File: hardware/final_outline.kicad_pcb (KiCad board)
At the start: 2 copper layers, 99.5 x 75 mm, 31 parts, among them P001 CANCONNECTOR, P002 CONN_01X14, P100 ISP, P101 DEBUG_LED, U401 MCP2551-I/SN, U403 LPC11C14, U501 MCP1755-33, U502 MCP1755-5, U503 Zsr1000gta

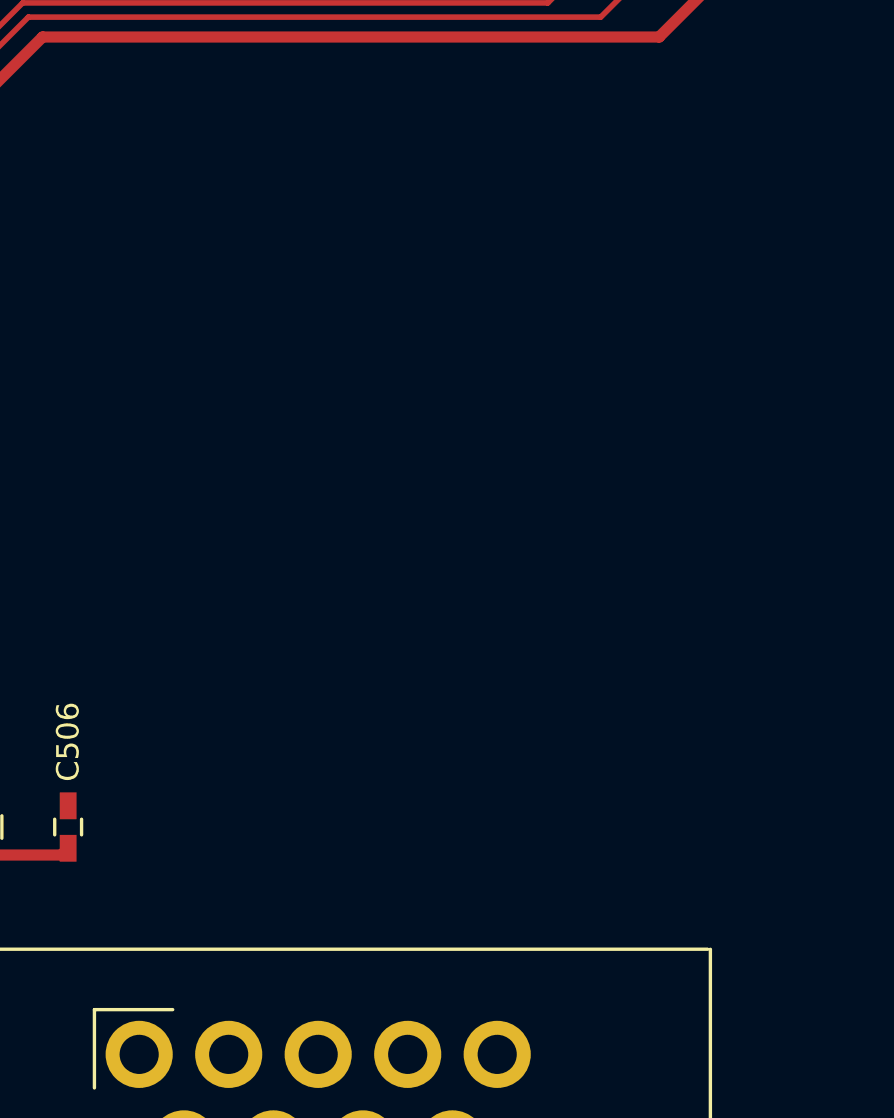
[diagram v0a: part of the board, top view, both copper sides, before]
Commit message: Fixed renaming issue in schematic, laid out components in pcb.
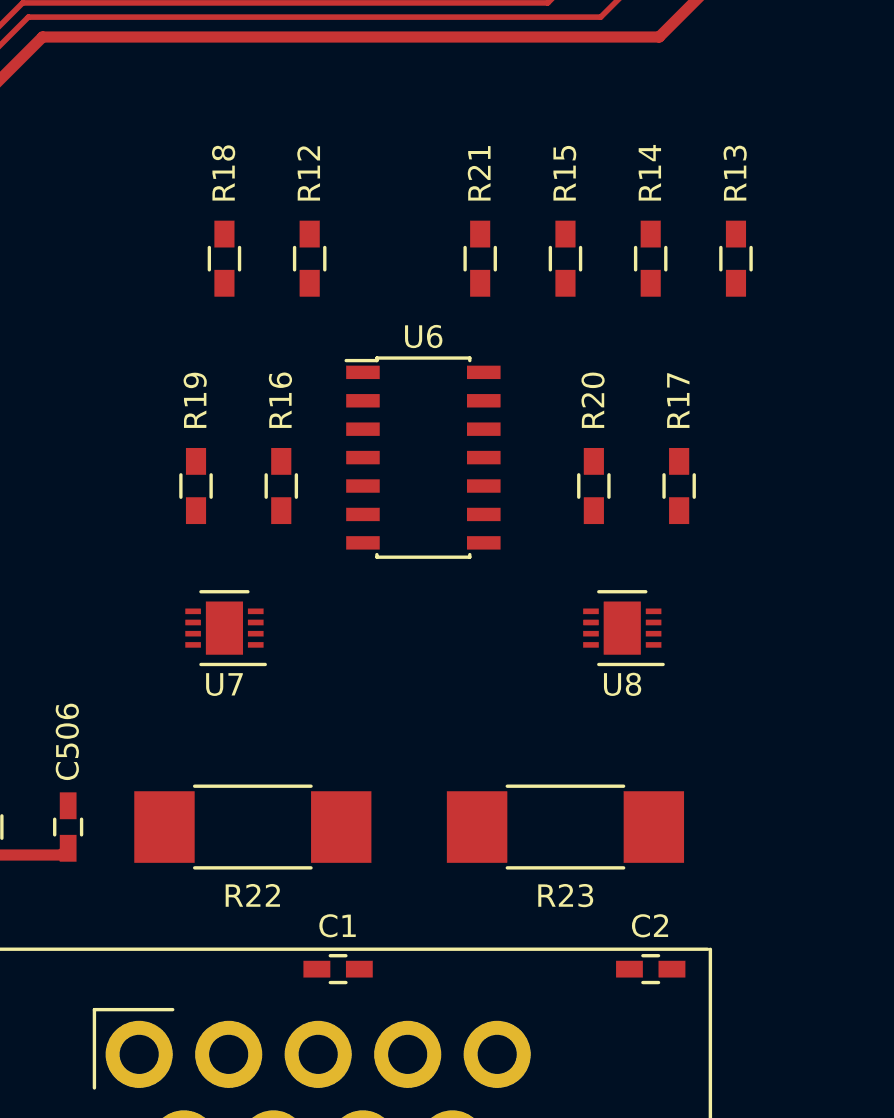
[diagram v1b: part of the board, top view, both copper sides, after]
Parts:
- added C1: 1uF, Capacitors_SMD:C_0603_HandSoldering, F.Cu at (171.4, 110.5)
- added C2: 1uF, Capacitors_SMD:C_0603_HandSoldering, F.Cu at (185.4, 110.5)
- added R12: 10k, Resistors_SMD:R_0603_HandSoldering, F.Cu at (170.2, 78.7)
- added R13: 10k, Resistors_SMD:R_0603_HandSoldering, F.Cu at (189.2, 78.7)
- added R14: 10k, Resistors_SMD:R_0603_HandSoldering, F.Cu at (185.4, 78.7)
- added R15: 10k, Resistors_SMD:R_0603_HandSoldering, F.Cu at (181.6, 78.7)
- added R16: 10k, Resistors_SMD:R_0603_HandSoldering, F.Cu at (168.9, 88.9)
- added R17: 10k, Resistors_SMD:R_0603_HandSoldering, F.Cu at (186.7, 88.9)
- added R18: 10k, Resistors_SMD:R_0603_HandSoldering, F.Cu at (166.4, 78.7)
- added R19: 10k, Resistors_SMD:R_0603_HandSoldering, F.Cu at (165.1, 88.9)
- added R20: 10k, Resistors_SMD:R_0603_HandSoldering, F.Cu at (182.9, 88.9)
- added R21: 10k, Resistors_SMD:R_0603_HandSoldering, F.Cu at (177.8, 78.7)
- added R22: 0.002, Resistors_SMD:R_2512_HandSoldering, F.Cu at (167.6, 104.1)
- added R23: 0.002, Resistors_SMD:R_2512_HandSoldering, F.Cu at (181.6, 104.1)
- added U6: TCA9543A, Housings_SOIC:SOIC-14_3.9x8.7mm_Pitch1.27mm, F.Cu at (175.3, 87.6)
- added U7: LTC2943, Housings_DFN_QFN:DFN-8-1EP_3x3mm_Pitch0.5mm, F.Cu at (166.4, 95.2)
- added U8: LTC2943, Housings_DFN_QFN:DFN-8-1EP_3x3mm_Pitch0.5mm, F.Cu at (184.2, 95.2)
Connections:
- P002 pad 1: Net-(P002-Pad1) -> /BACK_PANEL/CS_SENSE-
- P002 pad 2: Net-(P002-Pad2) -> /BACK_PANEL/CS_SENSE+
- P002 pad 4: Net-(P002-Pad4) -> /BACK_PANEL/LV_SENSE-
- P002 pad 5: Net-(P002-Pad5) -> /BACK_PANEL/LV_SENSE+
- P002 pad 6: Net-(P002-Pad6) -> /BACK_PANEL/CS_SENSE-
- P002 pad 7: Net-(P002-Pad7) -> /BACK_PANEL/CS_SENSE+
- P002 pad 8: Net-(P002-Pad8) -> /BACK_PANEL/LV_SENSE-
- P002 pad 9: Net-(P002-Pad9) -> /BACK_PANEL/LV_SENSE+
- U403 pad 15: /Micro_Controller/PIO0_4 -> /I2C Multiplexer and Gas Gauges/SCL
- U403 pad 16: /Micro_Controller/PIO0_5 -> /I2C Multiplexer and Gas Gauges/SDA

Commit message: Finished laying out PCB and completed traces.
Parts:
- moved C1 2.84 mm to (172.7, 108.0)
- moved C2 2.84 mm to (186.7, 108.0)
- moved R21 2.54 mm to (175.3, 78.7)
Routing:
- net /I2C Multiplexer and Gas Gauges/SCL: track 0.00 -> 115.0 mm, vias 0 -> 2
- net /I2C Multiplexer and Gas Gauges/SDA: track 0.00 -> 108.1 mm, vias 0 -> 2
- net +5V: track 113.2 -> 197.7 mm
- net /BACK_PANEL/CS_SENSE+: track 0.00 -> 26.9 mm
- net /BACK_PANEL/LV_SENSE+: track 0.00 -> 26.7 mm
- net /BACK_PANEL/LV_SENSE-: track 0.00 -> 26.5 mm
- net /BACK_PANEL/CS_SENSE-: track 0.00 -> 25.7 mm
- net Net-(R13-Pad2): track 0.00 -> 17.0 mm
- net Net-(R17-Pad2): track 0.00 -> 14.2 mm
- net Net-(R21-Pad2): track 0.00 -> 13.6 mm
- net Net-(R19-Pad2): track 0.00 -> 12.5 mm
- net Net-(R18-Pad2): track 0.00 -> 11.4 mm
- net GND: track 29.1 -> 39.3 mm, vias 6 -> 8
- net Net-(R20-Pad2): track 0.00 -> 9.54 mm
- net Net-(R16-Pad2): track 0.00 -> 8.69 mm
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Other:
- rule pad_to_mask_clearance: 0.2 -> 0.02

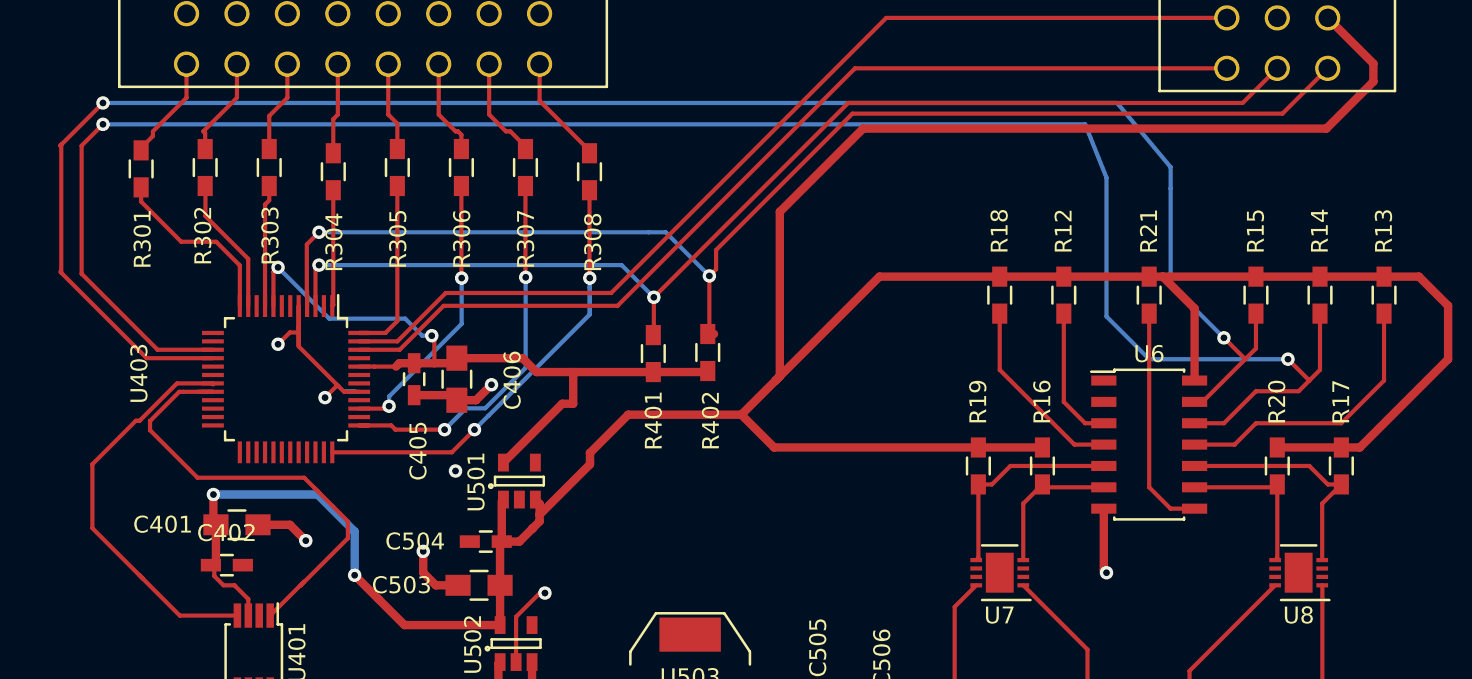
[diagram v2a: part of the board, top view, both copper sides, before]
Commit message: Finished PCB layout for real this time.
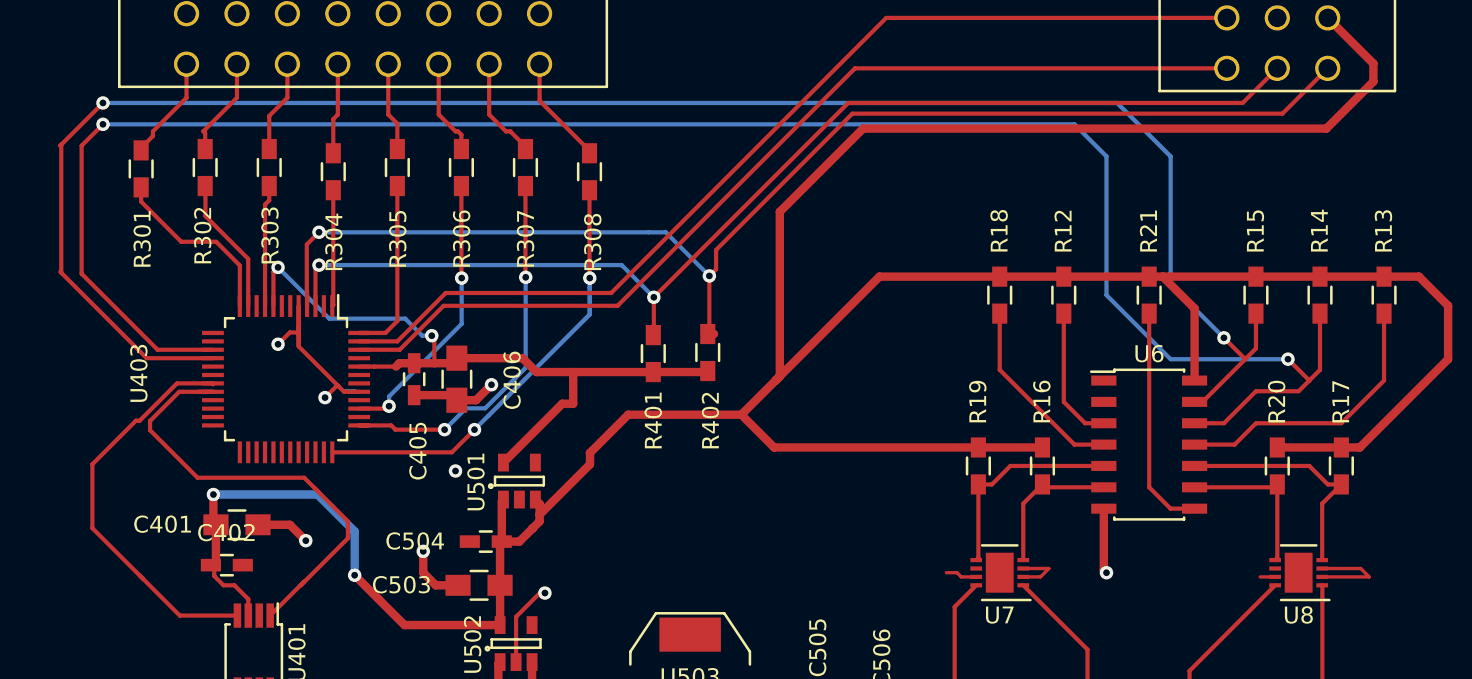
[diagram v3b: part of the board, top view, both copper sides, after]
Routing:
- net GND: track 39.3 -> 51.1 mm
- net /I2C Multiplexer and Gas Gauges/SCL: track 115.0 -> 114.1 mm
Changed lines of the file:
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@@
   (general
     (links 133)
-    (no_connects 6)
+    (no_connects 0)
     (area 102.424999 49.875 215 136.899792)
     (thickness 1.6)
     (drawings 6)
-    (tracks 432)
+    (tracks 441)
     (zones 0)
     (modules 48)
@@
   (segment (start 141.97 70.15) (end 141.97 70.3) (width 0.25) (layer F.Cu) (net 5))
   (segment (start 139 67.18) (end 141.97 70.15) (width 0.25) (layer F.Cu) (net 5))
+  (segment (start 182.75 95.5) (end 181.86 95.5) (width 0.2) (layer F.Cu) (net 6))
+  (segment (start 188.345 95.5) (end 187.845 95) (width 0.2) (layer F.Cu) (net 6))
+  (segment (start 187.845 95) (end 185.55 95) (width 0.2) (layer F.Cu) (net 6))
+  (segment (start 185.55 95.5) (end 188.345 95.5) (width 0.2) (layer F.Cu) (net 6))
+  (segment (start 163.83 95.25) (end 163.195 95.25) (width 0.2) (layer F.Cu) (net 6))
+  (segment (start 164.08 95.5) (end 163.83 95.25) (width 0.2) (layer F.Cu) (net 6))
+  (segment (start 164.97 95.5) (end 164.08 95.5) (width 0.2) (layer F.Cu) (net 6))
+  (segment (start 169.295 95) (end 168.795 95.5) (width 0.2) (layer F.Cu) (net 6))
+  (segment (start 168.795 95.5) (end 167.77 95.5) (width 0.2) (layer F.Cu) (net 6))
+  (segment (start 167.77 95) (end 169.295 95) (width 0.2) (layer F.Cu) (net 6))
   (segment (start 187.64 107.95) (end 188.595 107.95) (width 0.5) (layer F.Cu) (net 6))
   (via (at 192.405 104.14) (size 0.8) (drill 0.4) (layers F.Cu B.Cu) (net 6))
@@
   (segment (start 189.23 83.82) (end 186.69 86.36) (width 0.25) (layer F.Cu) (net 72))
   (segment (start 189.23 79.84) (end 189.23 80.01) (width 0.25) (layer F.Cu) (net 72))
-  (segment (start 113.03 68.58) (end 111.76 69.85) (width 0.25) (layer F.Cu) (net 73))
-  (segment (start 183.515 82.55) (end 175.26 82.55) (width 0.25) (layer B.Cu) (net 73))
-  (via (at 183.515 82.55) (size 0.8) (drill 0.4) (layers F.Cu B.Cu) (net 73))
-  (segment (start 184.785 83.82) (end 183.515 82.55) (width 0.25) (layer F.Cu) (net 73))
-  (segment (start 113.03 68.58) (end 171.45 68.58) (width 0.25) (layer B.Cu) (net 73))
-  (segment (start 172.72 71.755) (end 171.45 68.58) (width 0.25) (layer B.Cu) (net 73))
-  (segment (start 172.72 80.01) (end 172.72 71.755) (width 0.25) (layer B.Cu) (net 73))
-  (segment (start 175.26 82.55) (end 172.72 80.01) (width 0.25) (layer B.Cu) (net 73))
+  (segment (start 183.515 82.55) (end 176.53 82.55) (width 0.25) (layer B.Cu) (net 73))
   (via (at 113.03 68.58) (size 0.8) (drill 0.4) (layers F.Cu B.Cu) (net 73))
-  (segment (start 116.28 81.99) (end 119.57 81.99) (width 0.25) (layer F.Cu) (net 73))
+  (segment (start 119.57 81.99) (end 116.28 81.99) (width 0.25) (layer F.Cu) (net 73))
   (segment (start 111.76 77.47) (end 116.28 81.99) (width 0.25) (layer F.Cu) (net 73))
   (segment (start 111.76 69.85) (end 111.76 77.47) (width 0.25) (layer F.Cu) (net 73))
+  (segment (start 113.03 68.58) (end 111.76 69.85) (width 0.25) (layer F.Cu) (net 73))
+  (segment (start 172.72 70.485) (end 170.815 68.58) (width 0.25) (layer B.Cu) (net 73))
+  (segment (start 113.03 68.58) (end 170.815 68.58) (width 0.25) (layer B.Cu) (net 73))
+  (segment (start 183.515 82.55) (end 184.785 83.82) (width 0.25) (layer F.Cu) (net 73))
+  (via (at 183.515 82.55) (size 0.8) (drill 0.4) (layers F.Cu B.Cu) (net 73))
+  (segment (start 172.72 78.74) (end 172.72 70.485) (width 0.25) (layer B.Cu) (net 73))
+  (segment (start 176.53 82.55) (end 172.72 78.74) (width 0.25) (layer B.Cu) (net 73))
   (segment (start 185.42 79.84) (end 185.42 83.185) (width 0.25) (layer F.Cu) (net 73))
   (segment (start 179.705 86.36) (end 177.96 86.36) (width 0.25) (layer F.Cu) (net 73))
@@
   (segment (start 185.42 83.185) (end 184.785 83.82) (width 0.25) (layer F.Cu) (net 73))
   (segment (start 184.785 83.82) (end 184.15 84.455) (width 0.25) (layer F.Cu) (net 73))
+  (segment (start 176.53 78.105) (end 176.53 70.485) (width 0.25) (layer B.Cu) (net 74))
   (segment (start 110.55 77.41) (end 110.55 69.79) (width 0.25) (layer F.Cu) (net 74))
   (via (at 113.03 67.31) (size 0.8) (drill 0.4) (layers F.Cu B.Cu) (net 74))
-  (segment (start 176.53 71.12) (end 173.355 67.31) (width 0.25) (layer B.Cu) (net 74))
   (segment (start 113.03 67.31) (end 173.355 67.31) (width 0.25) (layer B.Cu) (net 74))
   (segment (start 179.705 81.28) (end 180.975 82.55) (width 0.25) (layer F.Cu) (net 74))
   (via (at 179.705 81.28) (size 0.8) (drill 0.4) (layers F.Cu B.Cu) (net 74))
   (segment (start 179.705 81.28) (end 176.53 78.105) (width 0.25) (layer B.Cu) (net 74))
-  (segment (start 176.53 78.105) (end 176.53 72.39) (width 0.25) (layer B.Cu) (net 74))
-  (segment (start 176.53 72.39) (end 176.53 71.12) (width 0.25) (layer B.Cu) (net 74))
   (segment (start 113.03 67.31) (end 110.49 69.85) (width 0.25) (layer F.Cu) (net 74))
   (segment (start 110.55 69.79) (end 110.49 69.85) (width 0.25) (layer F.Cu) (net 74))
+  (segment (start 173.355 67.31) (end 176.53 70.485) (width 0.25) (layer B.Cu) (net 74))
   (segment (start 119.57 82.49) (end 115.63 82.49) (width 0.25) (layer F.Cu) (net 74))
   (segment (start 115.63 82.49) (end 110.55 77.41) (width 0.25) (layer F.Cu) (net 74))

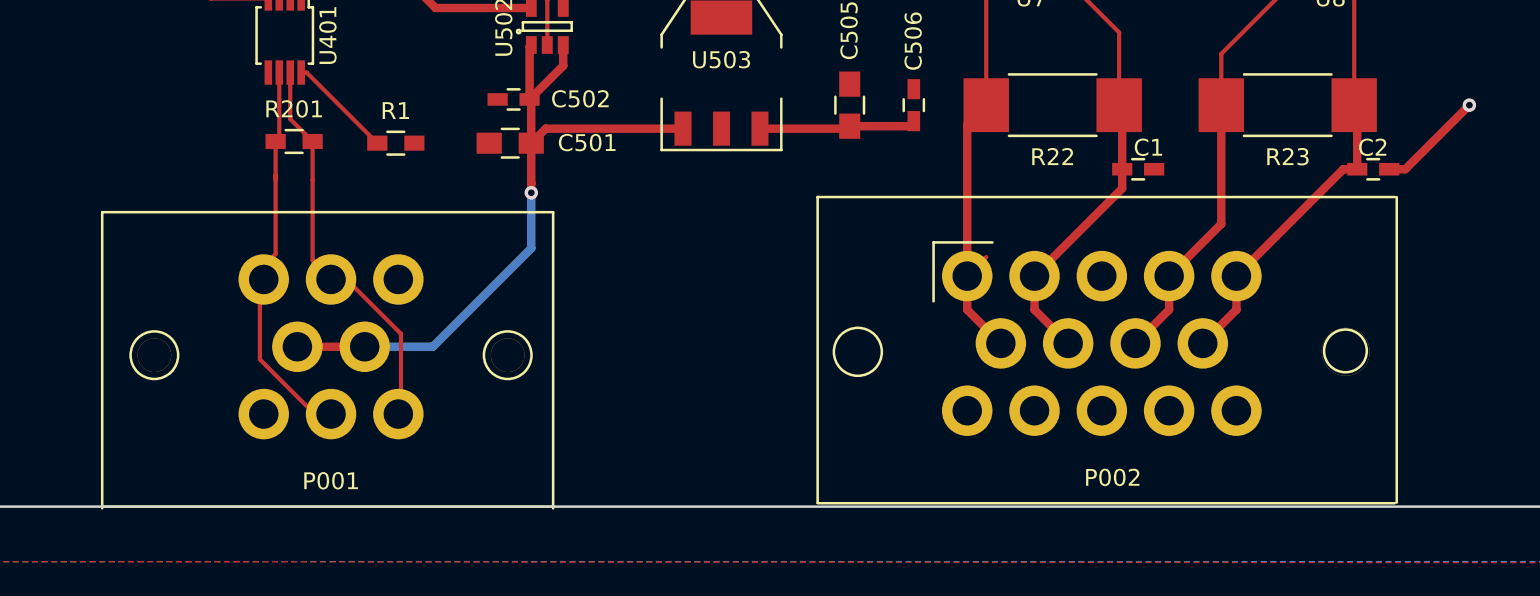
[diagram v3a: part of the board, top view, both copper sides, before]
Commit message: Fixed connector spacing.
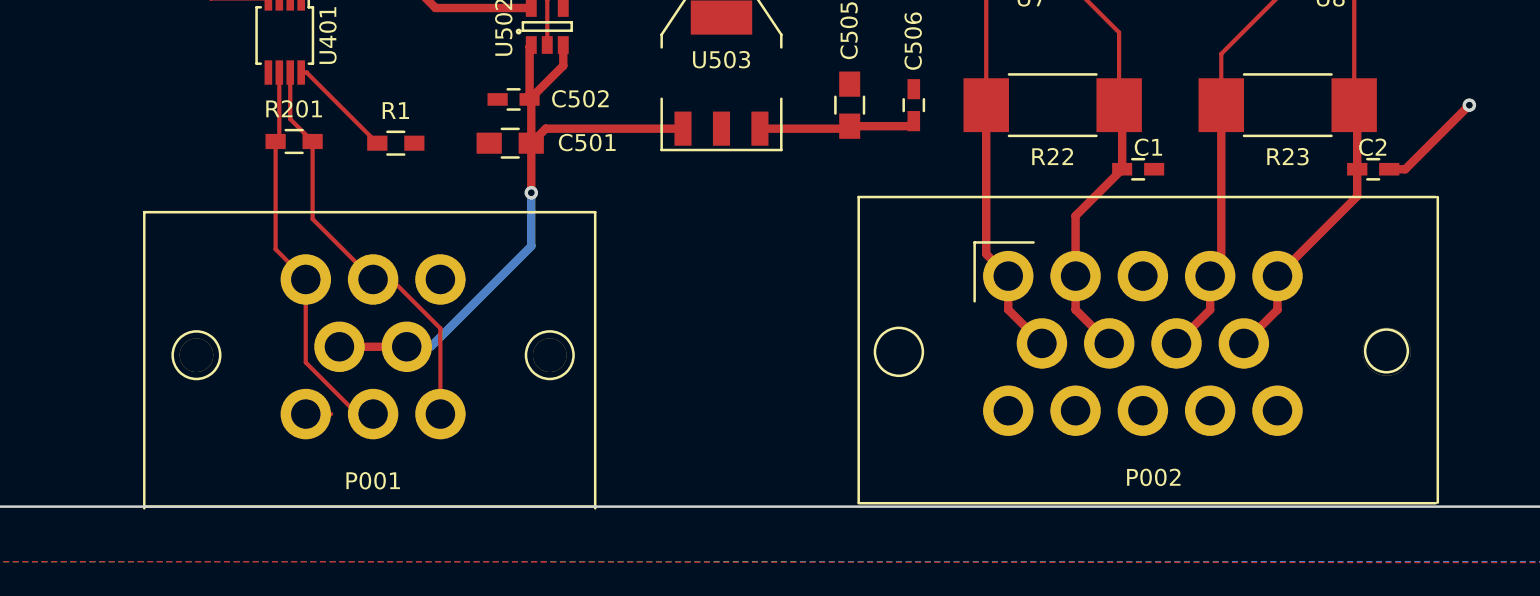
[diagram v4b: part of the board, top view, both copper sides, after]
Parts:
- moved P001 2.50 mm to (123.2, 122.5)
- moved P002 2.44 mm to (165.0, 114.3)
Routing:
- net +12V: track 42.1 -> 39.5 mm, vias 1 -> 2
- net /BACK_PANEL/CANH: track 23.2 -> 25.6 mm
- net /BACK_PANEL/LV_SENSE-: track 26.5 -> 24.6 mm
- net /BACK_PANEL/LV_SENSE+: track 26.7 -> 25.2 mm
- net /BACK_PANEL/CS_SENSE+: track 26.9 -> 25.9 mm
- net GND: track 51.1 -> 52.1 mm
